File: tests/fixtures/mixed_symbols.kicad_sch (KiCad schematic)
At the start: 14 parts, among them Q1 NPN, Q2 PNP, Q3 BF244A, SW1 SW_DPST_x2, T1 Transformer_1P_1S, U1 OP1177AR

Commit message: Draw JFETs from KiCad's own geometry so the gate is centred
circuitikz's njfet/pjfet place the gate a third of the way down the
channel and expose no way to centre it: the keys that move it (gate
height 2 / union height) also flatten the channel, which is why the
previous attempt was reverted.

JFETs are therefore drawn directly from KiCad's Transistor_FET geometry -
body circle, thick channel bar, filled gate arrow on the centre line, and
the stepped drain/source leads - anchored on the real pin positions and
scaled by SCALE, so it works at any orientation (gate on either side,
drain above or below) and every lead is straight. Bipolars and MOSFETs
still use circuitikz's shapes, which already centre their control pin.

Fixture refreshed with Q4 BF545B, exercising the description-based JFET
identification path alongside BF244A's part-number match.
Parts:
- added Q4: BF545B, Package_TO_SOT_SMD:SOT-23, symbol Transistor_FET:BF545B
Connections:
- net at B1.1 (N+), C2.2, L1.2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: now also Q4.1 (S), Q4.2 (D), Q4.3 (G)
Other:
- moved on the sheet: Q3
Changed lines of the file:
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@@
 	(paper "A4")
 	(junction
+		(at 129.54 144.78)
+		(diameter 0)
+		(color 0 0 0 0)
+	)
+	(junction
 		(at 105.41 90.17)
 		(diameter 0)
@@
 	)
 	(junction
+		(at 133.35 140.97)
+		(diameter 0)
+		(color 0 0 0 0)
+	)
+	(junction
 		(at 115.57 90.17)
 		(diameter 0)
@@
 	)
 	(junction
-		(at 133.35 144.78)
+		(at 144.78 140.97)
 		(diameter 0)
 		(color 0 0 0 0)
@@
 	)
 	(junction
-		(at 148.59 120.65)
-		(diameter 0)
-		(color 0 0 0 0)
-	)
-	(junction
 		(at 133.35 127)
 		(diameter 0)
@@
 	)
 	(junction
+		(at 135.89 140.97)
+		(diameter 0)
+		(color 0 0 0 0)
+	)
+	(junction
 		(at 105.41 107.95)
 		(diameter 0)
@@
 	)
 	(junction
+		(at 151.13 120.65)
+		(diameter 0)
+		(color 0 0 0 0)
+	)
+	(junction
 		(at 128.27 102.87)
 		(diameter 0)
@@
 	)
 	(junction
-		(at 140.97 127)
-		(diameter 0)
-		(color 0 0 0 0)
-	)
-	(junction
 		(at 88.9 107.95)
 		(diameter 0)
@@
 	)
 	(junction
+		(at 143.51 127)
+		(diameter 0)
+		(color 0 0 0 0)
+	)
+	(junction
 		(at 107.95 90.17)
 		(diameter 0)
@@
 	(wire
 		(pts
+			(xy 129.54 144.78) (xy 133.35 144.78)
+		)
+		(stroke
+			(width 0)
+			(type default)
+		)
+	)
+	(wire
+		(pts
 			(xy 102.87 90.17) (xy 105.41 90.17)
 		)
@@
 	(wire
 		(pts
-			(xy 133.35 127) (xy 140.97 127)
+			(xy 133.35 140.97) (xy 133.35 144.78)
+		)
+		(stroke
+			(width 0)
+			(type default)
+		)
+	)
+	(wire
+		(pts
+			(xy 133.35 127) (xy 143.51 127)
 		)
 		(stroke
@@
 	(wire
 		(pts
+			(xy 144.78 152.4) (xy 144.78 154.94)
+		)
+		(stroke
+			(width 0)
+			(type default)
+		)
+	)
+	(wire
+		(pts
 			(xy 105.41 90.17) (xy 105.41 95.25)
 		)
@@
 	(wire
 		(pts
+			(xy 135.89 140.97) (xy 144.78 140.97)
+		)
+		(stroke
+			(width 0)
+			(type default)
+		)
+	)
+	(wire
+		(pts
+			(xy 144.78 140.97) (xy 144.78 142.24)
+		)
+		(stroke
+			(width 0)
+			(type default)
+		)
+	)
+	(wire
+		(pts
 			(xy 88.9 102.87) (xy 88.9 107.95)
 		)
@@
 	(wire
 		(pts
+			(xy 135.89 147.32) (xy 135.89 140.97)
+		)
+		(stroke
+			(width 0)
+			(type default)
+		)
+	)
+	(wire
+		(pts
 			(xy 80.01 102.87) (xy 80.01 107.95)
 		)
@@
 	(wire
 		(pts
+			(xy 144.78 154.94) (xy 129.54 154.94)
+		)
+		(stroke
+			(width 0)
+			(type default)
+		)
+	)
+	(wire
+		(pts
 			(xy 161.29 107.95) (xy 161.29 115.57)
 		)
@@
 	(wire
 		(pts
+			(xy 137.16 147.32) (xy 135.89 147.32)
+		)
+		(stroke
+			(width 0)
+			(type default)
+		)
+	)
+	(wire
+		(pts
 			(xy 128.27 102.87) (xy 153.67 102.87)
 		)
@@
 	(wire
 		(pts
-			(xy 140.97 139.7) (xy 140.97 127)
-		)
-		(stroke
-			(width 0)
-			(type default)
-		)
-	)
-	(wire
-		(pts
-			(xy 125.73 144.78) (xy 133.35 144.78)
+			(xy 143.51 135.89) (xy 143.51 127)
+		)
+		(stroke
+			(width 0)
+			(type default)
+		)
+	)
+	(wire
+		(pts
+			(xy 125.73 144.78) (xy 129.54 144.78)
 		)
 		(stroke
@@
 	(wire
 		(pts
-			(xy 148.59 120.65) (xy 146.05 120.65)
+			(xy 129.54 154.94) (xy 129.54 144.78)
+		)
+		(stroke
+			(width 0)
+			(type default)
+		)
+	)
+	(wire
+		(pts
+			(xy 146.05 120.65) (xy 151.13 120.65)
 		)
 		(stroke
@@
 	(wire
 		(pts
-			(xy 133.35 127) (xy 133.35 144.78)
+			(xy 133.35 127) (xy 133.35 140.97)
 		)
 		(stroke
@@
 	(wire
 		(pts
-			(xy 148.59 120.65) (xy 148.59 134.62)
-		)
-		(stroke
-			(width 0)
-			(type default)
-		)
-	)
-	(wire
-		(pts
-			(xy 140.97 127) (xy 146.05 127)
+			(xy 151.13 120.65) (xy 151.13 130.81)
+		)
+		(stroke
+			(width 0)
+			(type default)
+		)
+	)
+	(wire
+		(pts
+			(xy 143.51 127) (xy 146.05 127)
 		)
 		(stroke
@@
 	(wire
 		(pts
-			(xy 133.35 144.78) (xy 148.59 144.78)
+			(xy 133.35 140.97) (xy 135.89 140.97)
 		)
 		(stroke
@@
 	(wire
 		(pts
+			(xy 144.78 140.97) (xy 151.13 140.97)
+		)
+		(stroke
+			(width 0)
+			(type default)
+		)
+	)
+	(wire
+		(pts
 			(xy 80.01 90.17) (xy 88.9 90.17)
 		)
@@
 	(wire
 		(pts
-			(xy 153.67 120.65) (xy 148.59 120.65)
+			(xy 153.67 120.65) (xy 151.13 120.65)
 		)
 		(stroke
@@
 	)
 	(symbol
+		(lib_id "Transistor_FET:BF545B")
+		(at 142.24 147.32 0)
+		(unit 1)
+		(body_style 1)
+		(exclude_from_sim no)
+		(in_bom yes)
+		(on_board yes)
+		(in_pos_files yes)
+		(dnp no)
+		(fields_autoplaced yes)
+		(property "Reference" "Q4"
+			(at 147.32 146.0499 0)
+			(show_name no)
+			(do_not_autoplace no)
+			(effects
+				(font
+					(size 1.27 1.27)
+				)
+				(justify left)
+			)
+		)
+		(property "Value" "BF545B"
+			(at 147.32 148.5899 0)
+			(show_name no)
+			(do_not_autoplace no)
+			(effects
+				(font
+					(size 1.27 1.27)
+				)
+				(justify left)
+			)
+		)
+		(property "Footprint" "Package_TO_SOT_SMD:SOT-23"
+			(at 147.32 149.225 0)
+			(hide yes)
+			(show_name no)
+			(do_not_autoplace no)
+			(effects
+				(font
+					(size 1.27 1.27)
+					(italic yes)
+				)
+				(justify left)
+			)
+		)
+		(property "Datasheet" "https://www.nxp.com/docs/en/data-sheet/BF545A_BF545B_BF545C.pdf"
+			(at 147.32 151.13 0)
+			(hide yes)
+			(show_name no)
+			(do_not_autoplace no)
+			(effects
+				(font
+					(size 1.27 1.27)
+				)
+				(justify left)
+			)
+		)
+		(property "Description" "15mA Idss, 30V Vgs, N-Channel JFET, SOT-23"
+			(at 142.24 147.32 0)
+			(hide yes)
+			(show_name no)
+			(do_not_autoplace no)
+			(effects
+				(font
+					(size 1.27 1.27)
+				)
+			)
+		)
+		(pin "2"
+		)
+		(pin "3"
+		)
+		(pin "1"
+		)
+		(instances
+			(project "Testing"
+				(path "/339a58e5-d3b3-42c1-934c-33ac2c9bf58f"
+					(reference "Q4")
+					(unit 1)
+				)
+			)
+		)
+	)
+	(symbol
 		(lib_id "Device:R")
 		(at 80.01 99.06 0)
@@
 		(property "Reference" "T1"
 			(at 115.5827 129.54 0)
+			(hide yes)
 			(show_name no)
 			(do_not_autoplace no)
@@
 		(property "Value" "Transformer_1P_1S"
 			(at 115.5827 132.08 0)
+			(hide yes)
 			(show_name no)
 			(do_not_autoplace no)
@@
 	(symbol
 		(lib_id "Transistor_FET:BF244A")
-		(at 146.05 139.7 0)
+		(at 148.59 135.89 0)
 		(unit 1)
 		(body_style 1)
@@
 		(fields_autoplaced yes)
 		(property "Reference" "Q3"
-			(at 151.13 138.4299 0)
+			(at 153.67 134.6199 0)
 			(show_name no)
 			(do_not_autoplace no)
@@
 		)
 		(property "Value" "BF244A"
-			(at 151.13 140.9699 0)
+			(at 153.67 137.1599 0)
 			(show_name no)
 			(do_not_autoplace no)
@@
 		)
 		(property "Footprint" "Package_TO_SOT_THT:TO-92_Inline"
-			(at 151.13 141.605 0)
+			(at 153.67 137.795 0)
 			(hide yes)
 			(show_name no)
@@
 		)
 		(property "Datasheet" "https://media.digikey.com/pdf/Data%20Sheets/Fairchild%20PDFs/BF244x.pdf"
-			(at 151.13 143.51 0)
+			(at 153.67 139.7 0)
 			(hide yes)
 			(show_name no)
@@
 		)
 		(property "Description" "50mA Id, 30V Vgs, N-Channel FET Transistor, TO-92"
-			(at 146.05 139.7 0)
+			(at 148.59 135.89 0)
 			(hide yes)
 			(show_name no)
@@
 		(property "Reference" "SW1"
 			(at 96.52 99.0599 90)
+			(hide yes)
 			(show_name no)
 			(do_not_autoplace no)
@@
 		(property "Value" "SW_DPST_x2"
 			(at 96.52 101.5999 90)
-			(show_name no)
-			(do_not_autoplace no)
+			(hide yes)
+			(show_name no)
+			(do_not_autoplace no)

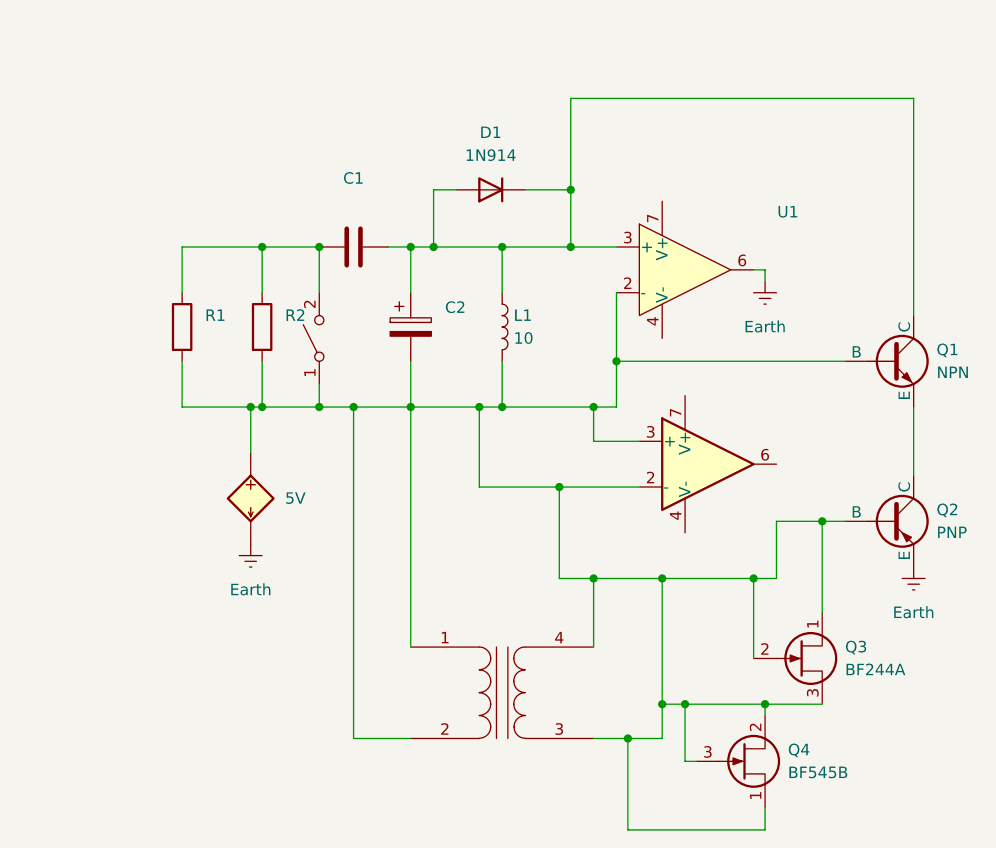
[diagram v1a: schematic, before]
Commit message: Draw polarity / winding-phase dots from the symbol graphics
KiCad marks polarity and winding phase with a filled circle in the symbol
art (the user's custom L_Polarized has one). The parser ignored symbol
graphics entirely, so the dot never reached the output.

Filled circles - fill type 'outline' - are now parsed into LibSymbol.dots
and carried onto Component.dots as absolute positions. Circles with no
fill or a background fill are body art (a source's envelope, a JFET's
circle) and are deliberately skipped. SymbolInstance.lib_point() factors
out the library-to-schematic transform that pin_position() already used,
so a dot rotates and mirrors with its symbol exactly like a pin.

The generator emits the dots from the shared graph rather than per symbol
type, so a dot survives whichever way its component is drawn. The detailed
alt text now states the marker too, since it is information a sighted
reader gets for free from the drawing.

Also maps the 'TR' reference prefix to TRANSFORMER, so the multi-winding
TEZ0.5-D-1 is described as a transformer instead of an unknown part.
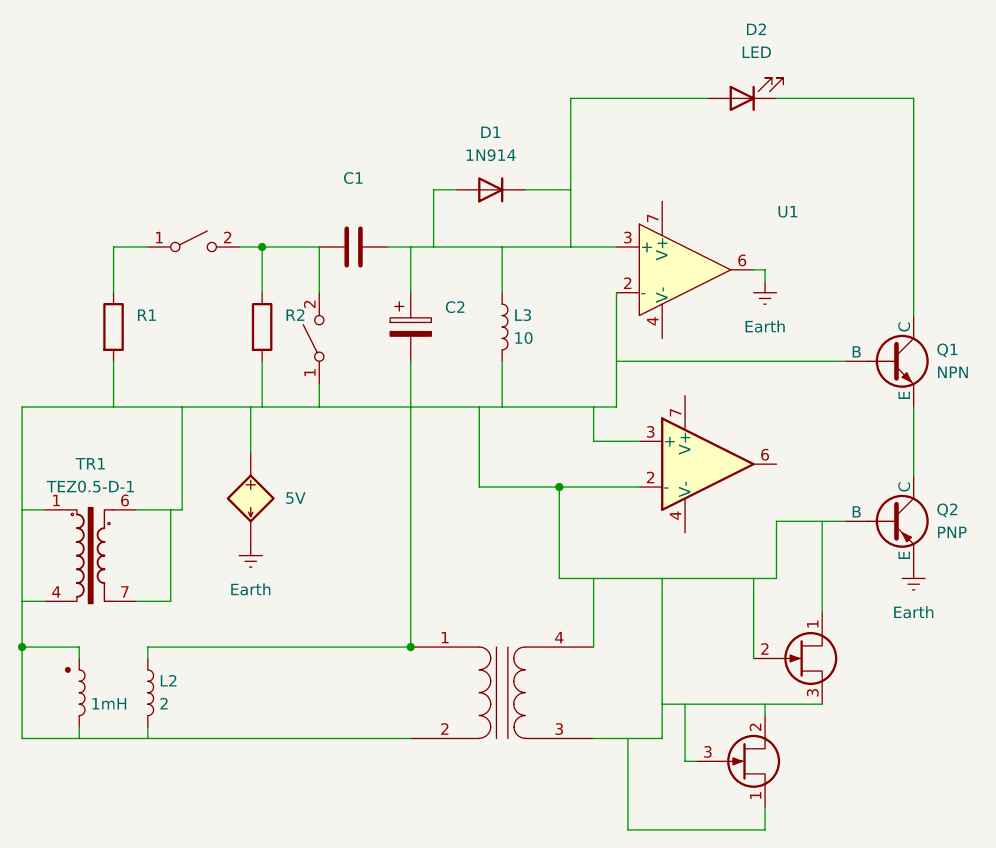
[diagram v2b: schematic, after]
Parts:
- added D2: LED, symbol Device:LED
- added L2: 2, symbol Device:L
- added L4: 1mH, symbol Polarized_L_Test:L_Polarized
- added SW2: SW_DPST_x2, symbol Switch:SW_DPST_x2
- added TR1: TEZ0.5-D-1, Transformer_THT:Transformer_Breve_TEZ-22x24, symbol Transformer:TEZ0.5-D-1
- renumbered L1 to L3
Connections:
- net at C1.1, R2.1, SW1.2 (B): now also SW2.2 (B); no longer R1.1
- new net: Q2.2 (B), U2.2 (-)
- new net: D2.1 (K), Q1.1 (C)
- new net: R1.1, SW2.1 (A)
- new net: L4.1, T1.2 (AB), U1.2 (-)
- new net: C2.2, L2.1, T1.1 (AA)
- new net: C1.2, U1.3 (+)
- now unconnected: B1.1 (N+), C2.1, D1.1 (K), D1.2 (A), L3.1, L3.2, Q1.2 (B), Q3.1 (D), Q3.2 (G), Q3.3 (S), Q4.1 (S), Q4.2 (D), Q4.3 (G), R1.2, R2.2, SW1.1 (A), T1.3 (SA), T1.4 (SB), U2.3 (+)
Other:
- moved on the sheet: R1
